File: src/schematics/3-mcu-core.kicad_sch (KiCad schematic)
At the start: 110 parts, among them Q301 NX6008NBKW, U301 PIC32CX1025SG41100-I/E5X, U302 AP22653AW6

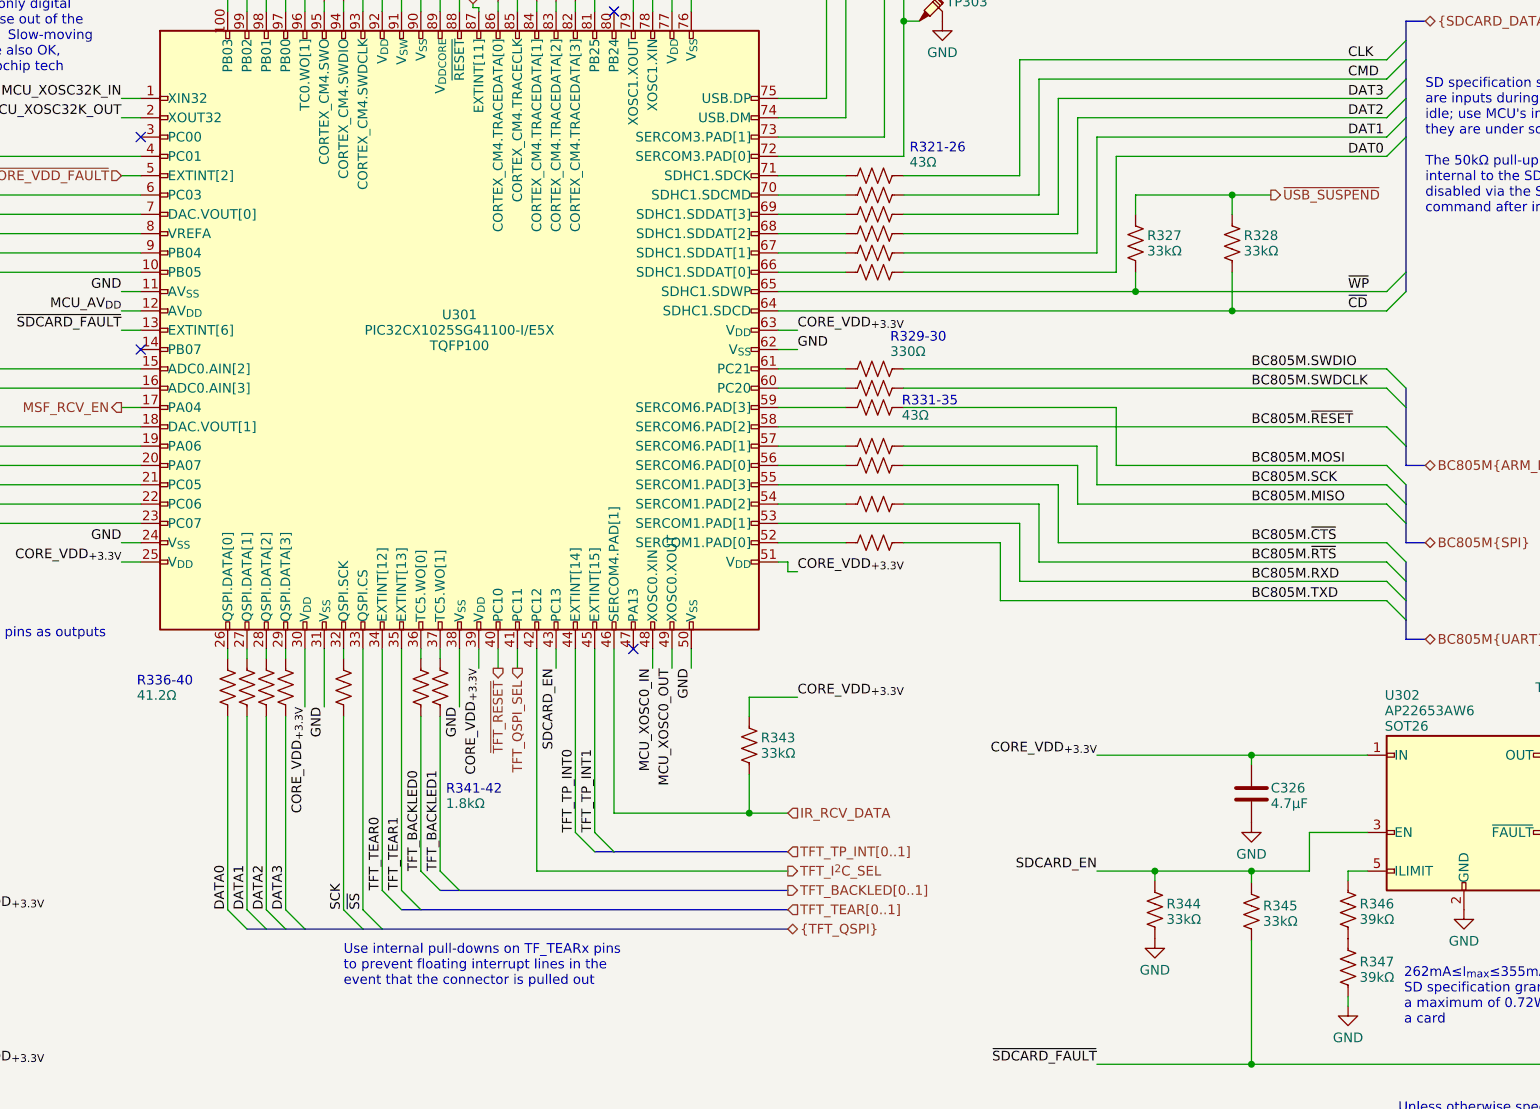
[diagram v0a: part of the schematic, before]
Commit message: Updated reference designators after removing R320.
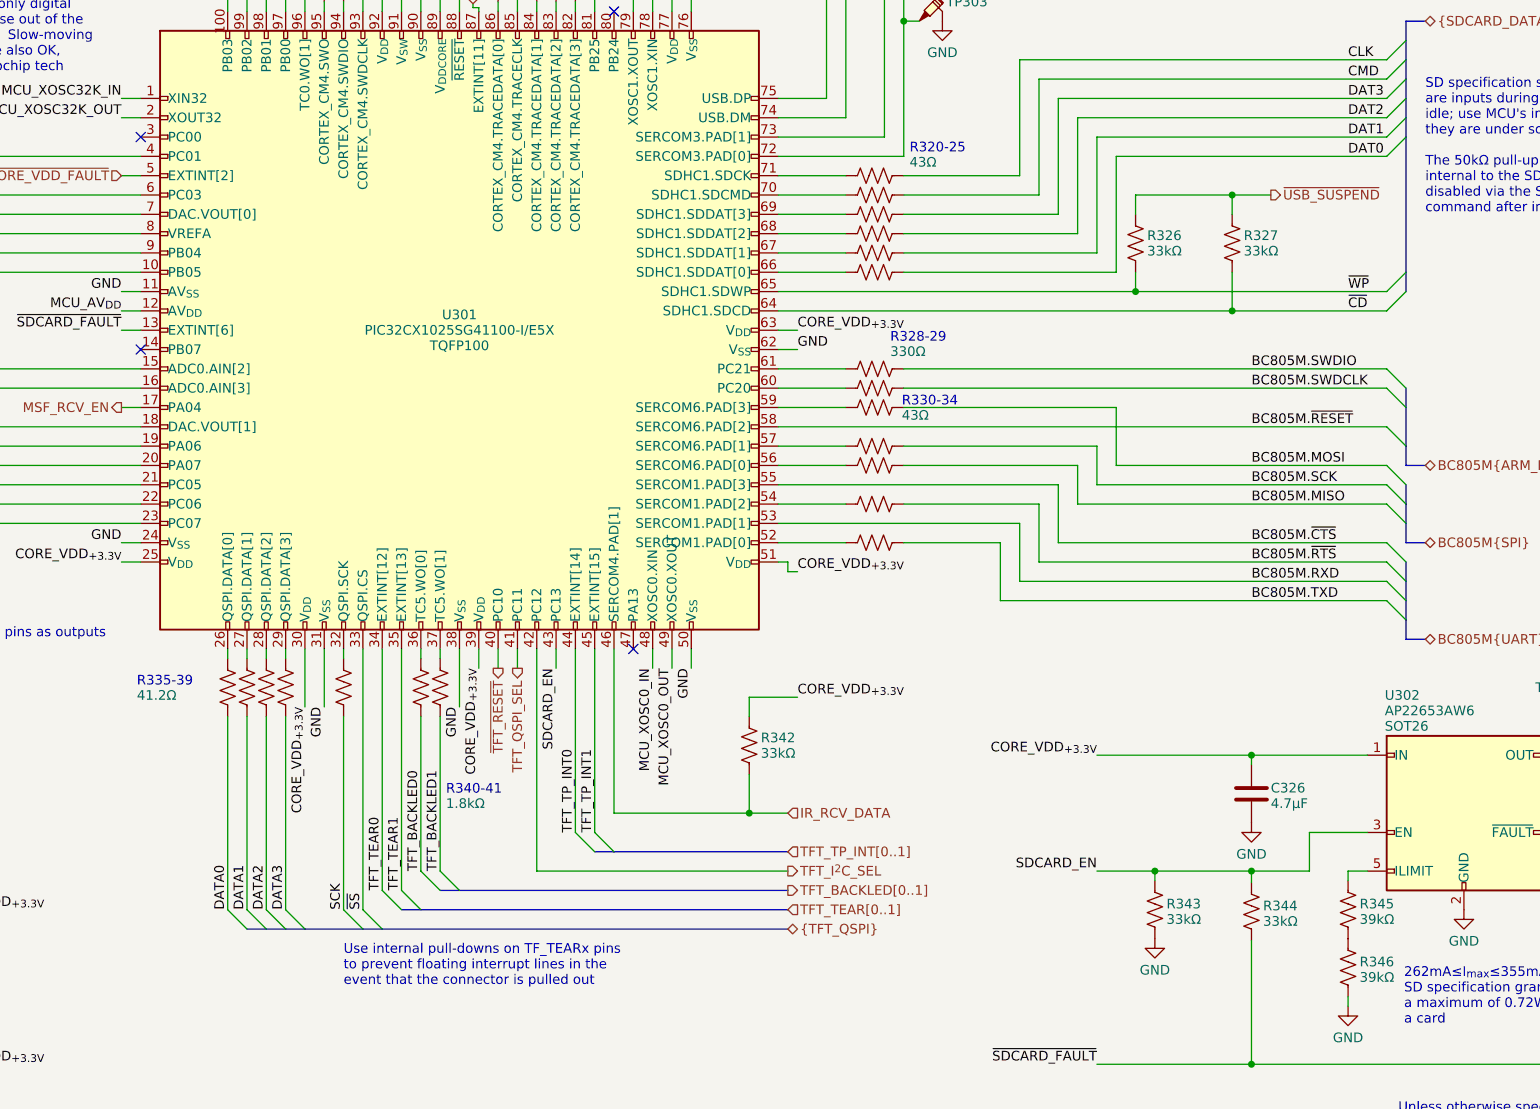
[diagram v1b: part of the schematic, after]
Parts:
- renumbered R321 to R320, R322 to R321, R323 to R322, R324 to R323, R325 to R324, R326 to R325, R327 to R326, R328 to R327, R329 to R328, R330 to R329, R331 to R330, R332 to R331, R333 to R332, R334 to R333, R335 to R334, R336 to R335, R337 to R336, R338 to R337, R339 to R338, R340 to R339, R341 to R340, R342 to R341, R343 to R342, R344 to R343, R345 to R344, R346 to R345, R347 to R346
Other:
- note added: "R320-25"
- note added: "R328-29"
- note added: "R330-34"
- note added: "R335-39"
- note added: "R340-41"
- note removed: "R321-26"
- note removed: "R329-30"
- note removed: "R331-35"
- note removed: "R336-40"
- note removed: "R341-42"

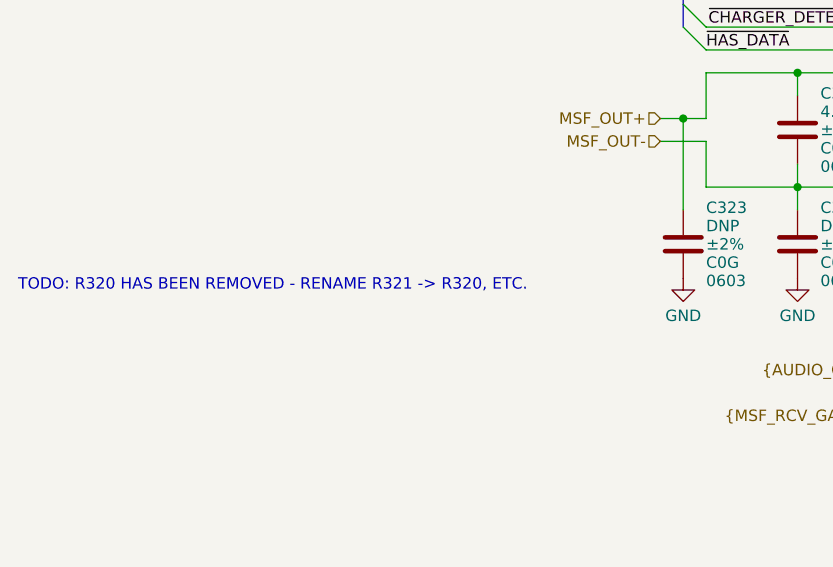
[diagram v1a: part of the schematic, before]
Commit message: Updated reference designators on the schematic after PCB layout amendments finalised.
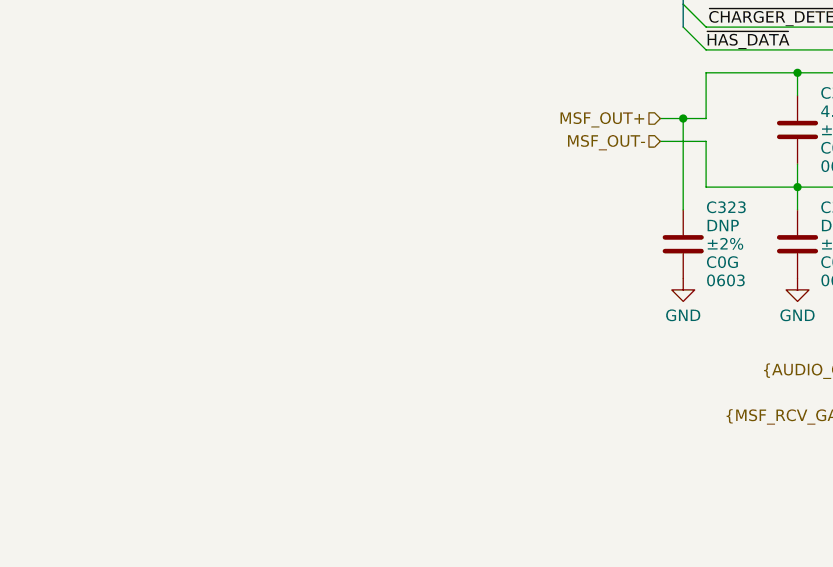
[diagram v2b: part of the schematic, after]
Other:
- note removed: "TODO: R320 HAS BEEN REMOVED - RENAME R321 -> R320, ETC."
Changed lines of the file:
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@@
-    (effects (font (size 1.27 1.27)) (justify left bottom))
-  )
-  (text "TODO: R320 HAS BEEN REMOVED - RENAME R321 -> R320, ETC."
-    (at -7.874 171.704 0)
     (effects (font (size 1.27 1.27)) (justify left bottom))
   )

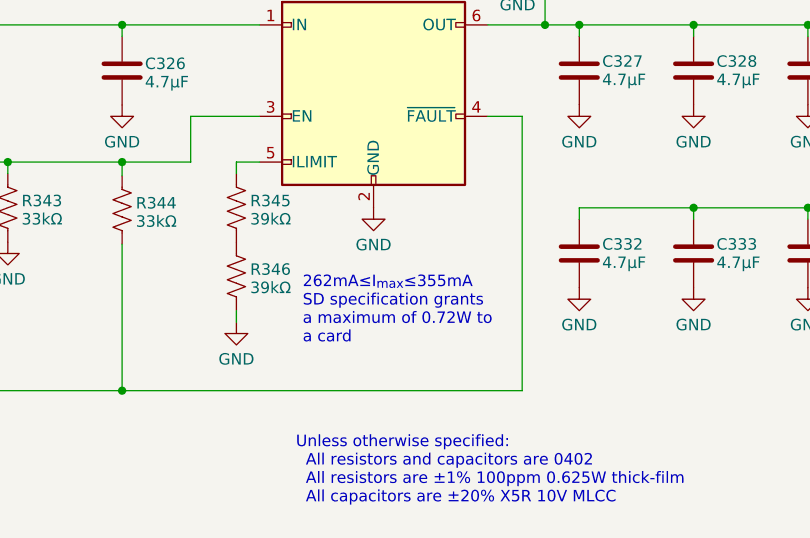
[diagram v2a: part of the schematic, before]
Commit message: Updated to allow up to 1.44W for the SD card, which is actually what UHS-I specifications are measured at; 0.72W is the limit for the default speed mode / driver strength.
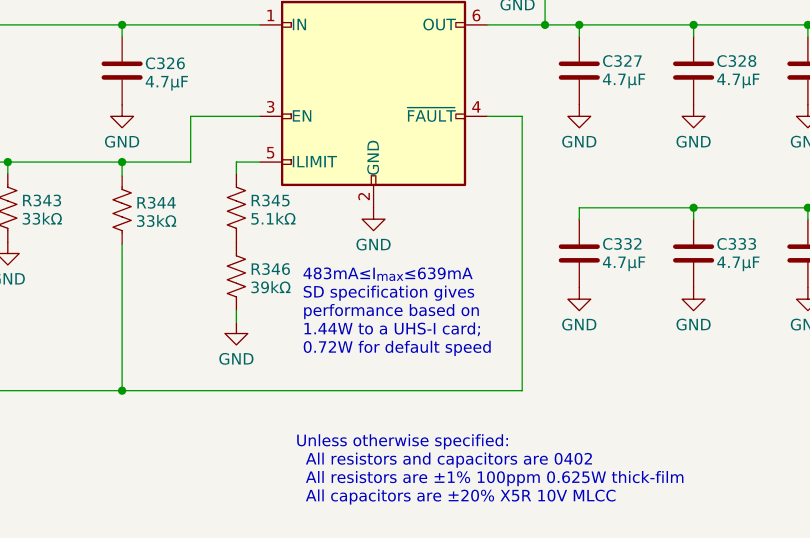
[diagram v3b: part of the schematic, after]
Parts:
- R345: value 39kΩ -> 5.1kΩ; Label 39kΩ±1% 0.0625W -> 5.1kΩ±1% 0.0625W; Manufacturer Yageo -> Walsin; Manufacturer2PartNumber AC0402DR-0739KL -> RC0402FR-075K1L; ManufacturerPartNumber RC0402FR-0739KL -> WR04X5101FTL
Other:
- note added: "483mA≤I_{max}≤639mA SD specification gives performance based on 1.44W to a UHS-I card; 0.72W for default speed"
- note removed: "262mA≤I_{max}≤355mA SD specification grants a maximum of 0.72W to a card"
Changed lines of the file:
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@@
     (effects (font (size 2.54 2.54)) (justify left bottom))
   )
-  (text "262mA≤I_{max}≤355mA\nSD specification grants\na maximum of 0.72W to\na card"
-    (at 302.006 243.84 0)
+  (text "483mA≤I_{max}≤639mA\nSD specification gives\nperformance based on\n1.44W to a UHS-I card;\n0.72W for default speed"
+    (at 302.006 245.11 0)
     (effects (font (size 1.27 1.27)) (justify left bottom))
   )
@@
       (effects (font (size 1.27 1.27)) (justify left))
     )
-    (property "Value" "39kΩ" (at 296.164 229.87 0)
+    (property "Value" "5.1kΩ" (at 296.164 229.87 0)
       (effects (font (size 1.27 1.27)) (justify left))
     )
@@
       (effects (font (size 1.27 1.27)) (justify left) hide)
     )
-    (property "Label" "39kΩ±1% 0.0625W" (at 296.418 230.124 0)
+    (property "Label" "5.1kΩ±1% 0.0625W" (at 296.418 230.124 0)
       (effects (font (size 1.27 1.27)) (justify left) hide)
     )
@@
       (effects (font (size 1.27 1.27)) (justify left) hide)
     )
-    (property "Manufacturer" "Yageo" (at 294.64 228.6 0)
-      (effects (font (size 1.27 1.27)) (justify left) hide)
-    )
-    (property "ManufacturerPartNumber" "RC0402FR-0739KL" (at 294.64 228.6 0)
+    (property "Manufacturer" "Walsin" (at 294.64 228.6 0)
+      (effects (font (size 1.27 1.27)) (justify left) hide)
+    )
+    (property "ManufacturerPartNumber" "WR04X5101FTL" (at 294.64 228.6 0)
       (effects (font (size 1.27 1.27)) (justify left) hide)
     )
@@
       (effects (font (size 1.27 1.27)) (justify left) hide)
     )
-    (property "Manufacturer2PartNumber" "AC0402DR-0739KL" (at 294.64 228.6 0)
-      (effects (font (size 1.27 1.27)) (justify left) hide)
-    )
+    (property "Manufacturer2PartNumber" "RC0402FR-075K1L" (at 294.64 228.6 0)
+      (effects (font (size 1.27 1.27)) (justify left) hide)
+    )

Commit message: PCB routing.
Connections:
- net SDCARD_EN: now also U301.45 (PC15); no longer U301.43 (PC13)
- net TFT_TP_INT0: now also U301.43 (PC13); no longer U301.44 (PC14)
- net TFT_TP_INT1: now also U301.44 (PC14); no longer U301.45 (PC15)
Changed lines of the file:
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@@
     (stroke (width 0) (type default))
   )
-  (bus_entry (at 195.58 220.98) (size -2.54 -2.54)
+  (bus_entry (at 193.04 220.98) (size -2.54 -2.54)
     (stroke (width 0) (type default))
   )
@@
     (stroke (width 0) (type default))
   )
-  (bus_entry (at 198.12 220.98) (size -2.54 -2.54)
+  (bus_entry (at 195.58 220.98) (size -2.54 -2.54)
     (stroke (width 0) (type default))
   )
@@
     (stroke (width 0) (type default))
   )
+  (bus (pts (xy 195.58 220.98) (xy 220.98 220.98))
+    (stroke (width 0) (type default))
+  )
   (wire (pts (xy 162.56 25.4) (xy 175.26 25.4))
     (stroke (width 0) (type default))
@@
     (stroke (width 0) (type default))
   )
-  (bus (pts (xy 195.58 220.98) (xy 198.12 220.98))
-    (stroke (width 0) (type default))
-  )
   (wire (pts (xy 205.74 68.58) (xy 294.64 68.58))
     (stroke (width 0) (type default))
@@
     (stroke (width 0) (type default))
   )
-  (bus (pts (xy 198.12 220.98) (xy 220.98 220.98))
-    (stroke (width 0) (type default))
-  )
   (wire (pts (xy 170.18 194.31) (xy 170.18 226.06))
     (stroke (width 0) (type default))
@@
     (stroke (width 0) (type default))
   )
-  (wire (pts (xy 190.5 194.31) (xy 190.5 196.85))
+  (wire (pts (xy 195.58 194.31) (xy 195.58 196.85))
     (stroke (width 0) (type default))
   )
@@
     (stroke (width 0) (type default))
   )
+  (bus (pts (xy 193.04 220.98) (xy 195.58 220.98))
+    (stroke (width 0) (type default))
+  )
   (wire (pts (xy 187.96 109.22) (xy 187.96 110.49))
     (stroke (width 0) (type default))
@@
     (stroke (width 0) (type default))
   )
-  (wire (pts (xy 193.04 218.44) (xy 193.04 194.31))
+  (wire (pts (xy 190.5 218.44) (xy 190.5 194.31))
     (stroke (width 0) (type default))
   )
@@
     (stroke (width 0) (type default))
   )
-  (wire (pts (xy 195.58 194.31) (xy 195.58 218.44))
+  (wire (pts (xy 193.04 194.31) (xy 193.04 218.44))
     (stroke (width 0) (type default))
   )
@@
     (effects (font (size 1.27 1.27)) (justify left bottom))
   )
-  (label "TFT_TP_INT1" (at 195.58 218.44 90) (fields_autoplaced)
+  (label "TFT_TP_INT1" (at 193.04 218.44 90) (fields_autoplaced)
     (effects (font (size 1.27 1.27)) (justify left bottom))
   )
@@
     (effects (font (size 1.27 1.27)) (justify left bottom))
   )
-  (label "SDCARD_EN" (at 190.5 196.85 270) (fields_autoplaced)
+  (label "SDCARD_EN" (at 195.58 196.85 270) (fields_autoplaced)
     (effects (font (size 1.27 1.27)) (justify right bottom))
   )
@@
     (effects (font (size 1.27 1.27)) (justify left bottom))
   )
-  (label "TFT_TP_INT0" (at 193.04 218.44 90) (fields_autoplaced)
+  (label "TFT_TP_INT0" (at 190.5 218.44 90) (fields_autoplaced)
     (effects (font (size 1.27 1.27)) (justify left bottom))
   )
@@
     (pin "92")
     (pin "91")
-    (pin "43")
+    (pin "43" (alternate "EXTINT[13]"))
     (pin "65" (alternate "SDHC1.SDWP"))
     (pin "29" (alternate "QSPI.DATA[3]"))
@@
     (pin "84" (alternate "CORTEX_CM4.TRACEDATA[1]"))
     (pin "72" (alternate "SERCOM3.PAD[0]"))
-    (pin "45" (alternate "EXTINT[15]"))
+    (pin "45")
     (pin "7" (alternate "DAC.VOUT[0]"))
     (pin "54" (alternate "SERCOM1.PAD[2]"))

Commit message: PCB routing.
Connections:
- net TFT_BACKLED0: now also R341.1; no longer R340.1
- net TFT_BACKLED1: now also R340.1; no longer R341.1
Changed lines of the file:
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@@
     (effects (font (size 1.27 1.27)) (justify left bottom))
   )
-  (label "TFT_BACKLED0" (at 172.72 223.52 90) (fields_autoplaced)
+  (label "TFT_BACKLED0" (at 175.26 223.52 90) (fields_autoplaced)
     (effects (font (size 1.27 1.27)) (justify left bottom))
   )
@@
     (effects (font (size 1.27 1.27)) (justify right bottom))
   )
-  (label "TFT_BACKLED1" (at 175.26 223.52 90) (fields_autoplaced)
+  (label "TFT_BACKLED1" (at 172.72 223.52 90) (fields_autoplaced)
     (effects (font (size 1.27 1.27)) (justify left bottom))
   )

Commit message: PCB routing.
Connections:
- net TFT_TEAR0: now also U301.35 (PB13); no longer U301.34 (PB12)
- net TFT_TEAR1: now also U301.34 (PB12); no longer U301.35 (PB13)
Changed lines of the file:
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@@
     (effects (font (size 1.27 1.27)) (justify right bottom))
   )
-  (label "TFT_TEAR0" (at 167.64 226.06 90) (fields_autoplaced)
+  (label "TFT_TEAR0" (at 170.18 226.06 90) (fields_autoplaced)
     (effects (font (size 1.27 1.27)) (justify left bottom))
   )
@@
     (effects (font (size 1.27 1.27)) (justify left bottom))
   )
-  (label "TFT_TEAR1" (at 170.18 226.06 90) (fields_autoplaced)
+  (label "TFT_TEAR1" (at 167.64 226.06 90) (fields_autoplaced)
     (effects (font (size 1.27 1.27)) (justify left bottom))
   )

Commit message: PCB routing.
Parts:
- TP302, TP303: footprint restall-generic-test:testpoint-SP3050A-with-short-gnd -> restall-generic-test:th-testpoint-0.5mm-with-short-gnd
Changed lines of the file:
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@@
       (effects (font (size 1.27 1.27)) (justify right) hide)
     )
-    (property "Footprint" "restall-generic-test:testpoint-SP3050A-with-short-gnd" (at 243.332 111.76 0)
+    (property "Footprint" "restall-generic-test:th-testpoint-0.5mm-with-short-gnd" (at 243.332 111.76 0)
       (effects (font (size 1.27 1.27)) (justify right) hide)
     )
@@
       (effects (font (size 1.27 1.27)) (justify right) hide)
     )
-    (property "Footprint" "restall-generic-test:testpoint-SP3050A-with-short-gnd" (at 236.22 98.806 0)
-      (effects (font (size 1.27 1.27)) (justify right) hide)
-    )
+    (property "Footprint" "restall-generic-test:th-testpoint-0.5mm-with-short-gnd" (at 236.22 98.806 0)
+      (effects (font (size 1.27 1.27)) (justify right) hide)
+    )

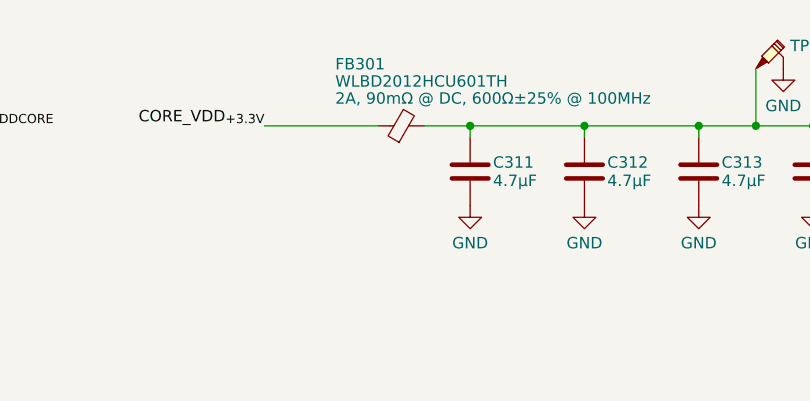
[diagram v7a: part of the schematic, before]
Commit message: PCB routing.  Fixed most of the DRC violations.
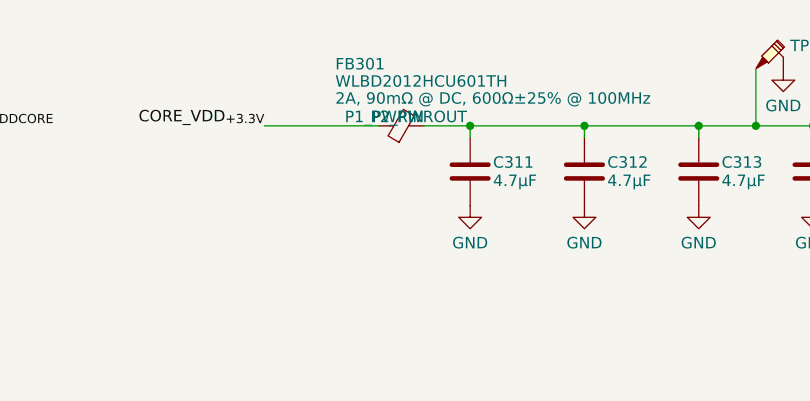
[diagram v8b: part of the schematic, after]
